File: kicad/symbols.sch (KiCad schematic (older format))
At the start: 70 parts

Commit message: stackup
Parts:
- added logo1306: stackup, servo:layers_stackup, symbol servo:logo
- H1301, H1302, H1303, H1304, H1305, H1306, H1307, H1308, H1309, H1310, H1311, H1312, H1313, H1314, H1315, H1316, H1317, H1318, H1319, H1320, H1321, H1322, H1323, H1324, H1325, H1326, H1327, H1328, H1329, H1330, H1331, H1332, H1333, H1334, H1335, H1336, H1337, H1338, H1339, H1340, H1341, H1342, H1343, H1344, H1345, H1346, H1347, H1348, H1349, H1350, H1351, H1352, H1353, H1354, H1355, H1356, H1357, H1358: price@10 (none) -> 0

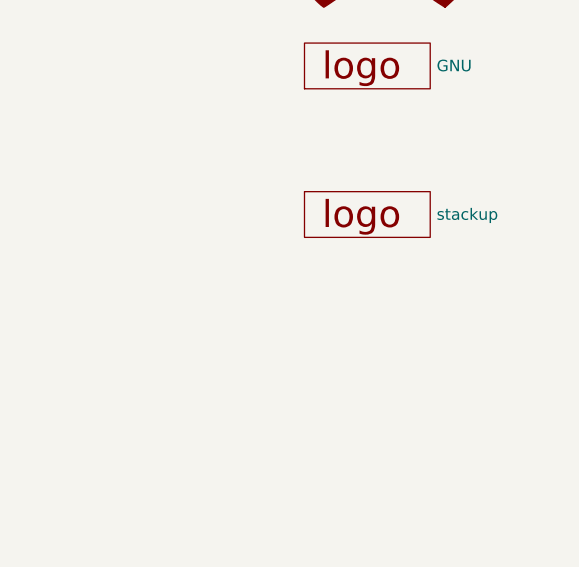
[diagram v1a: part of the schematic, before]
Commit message: changes in footprints
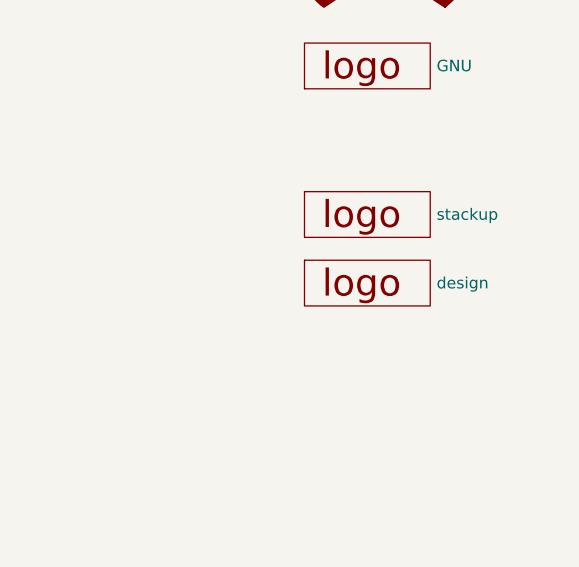
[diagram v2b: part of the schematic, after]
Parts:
- added logo1307: design, servo:layers_design, symbol servo:logo
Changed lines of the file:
@@
+	1    0    0    -1
+$EndComp
+$Comp
+L servo:logo logo1307
+U 1 1 5E5C71DB
+P 13250 6200
+F 0 "logo1307" H 13250 6400 50  0001 C CNN
+F 1 "design" H 13578 6200 50  0000 L CNN
+F 2 "servo:layers_design" H 13250 6200 50  0001 C CNN
+F 3 "~" H 13250 6200 50  0001 C CNN
+F 4 "stackup" H -150 3250 50  0001 C CNN "Description"
+F 5 "-" H -150 3250 50  0001 C CNN "PartNumber"
+F 6 "0" H -150 3250 50  0001 C CNN "price@10"
+	1    13250 6200
 	1    0    0    -1
 $EndComp

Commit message: fine imprivements
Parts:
- H1302, H1304, H1306, H1308: footprint servo:Fiducial_1mm_Dia_2.54mm_Outer_CopperBottom -> servo:Fiducial_1mm_Dia_2.54mm_Outer_CopperTop
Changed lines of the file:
@@
 F 0 "H1302" H 4250 2946 50  0000 L CNN
 F 1 "fiducials" H 4250 2855 50  0000 L CNN
-F 2 "servo:Fiducial_1mm_Dia_2.54mm_Outer_CopperBottom" H 4150 2900 50  0001 C CNN
+F 2 "servo:Fiducial_1mm_Dia_2.54mm_Outer_CopperTop" H 4150 2900 50  0001 C CNN
 F 3 "~" H 4150 2900 50  0001 C CNN
 F 4 "fiducials" H 0   0   50  0001 C CNN "Description"
@@
 F 0 "H1304" H 4950 2946 50  0000 L CNN
 F 1 "fiducials" H 4950 2855 50  0000 L CNN
-F 2 "servo:Fiducial_1mm_Dia_2.54mm_Outer_CopperBottom" H 4850 2900 50  0001 C CNN
+F 2 "servo:Fiducial_1mm_Dia_2.54mm_Outer_CopperTop" H 4850 2900 50  0001 C CNN
 F 3 "~" H 4850 2900 50  0001 C CNN
 F 4 "fiducials" H 0   0   50  0001 C CNN "Description"
@@
 F 0 "H1306" H 5600 2946 50  0000 L CNN
 F 1 "fiducials" H 5600 2855 50  0000 L CNN
-F 2 "servo:Fiducial_1mm_Dia_2.54mm_Outer_CopperBottom" H 5500 2900 50  0001 C CNN
+F 2 "servo:Fiducial_1mm_Dia_2.54mm_Outer_CopperTop" H 5500 2900 50  0001 C CNN
 F 3 "~" H 5500 2900 50  0001 C CNN
 F 4 "fiducials" H 0   0   50  0001 C CNN "Description"
@@
 F 0 "H1308" H 6250 2946 50  0000 L CNN
 F 1 "fiducials" H 6250 2855 50  0000 L CNN
-F 2 "servo:Fiducial_1mm_Dia_2.54mm_Outer_CopperBottom" H 6150 2900 50  0001 C CNN
+F 2 "servo:Fiducial_1mm_Dia_2.54mm_Outer_CopperTop" H 6150 2900 50  0001 C CNN
 F 3 "~" H 6150 2900 50  0001 C CNN
 F 4 "fiducials" H 0   0   50  0001 C CNN "Description"

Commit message: gerbers + pnp + bom ready
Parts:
- removed logo1304: GNU, Symbol:Symbol_GNU-Logo_SilkscreenTop, symbol servo:logo
- added logo1308: pslavkin_top, servo:logo_pslavkin, symbol servo:logo
- logo1302: value pslavkin -> pslavkin_bottom
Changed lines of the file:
@@
 L servo:high_voltage ref1302
 U 1 1 5E38C9D6
-P 13200 3450
-F 0 "ref1302" V 13110 3450 50  0001 C CNN
-F 1 "high_voltage" V 13290 3450 50  0001 C CNN
-F 2 "servo:Symbol_Highvoltage_Type1_CopperTop_Small" H 13400 3950 50  0001 C CNN
-F 3 "~" H 13600 3350 50  0001 C CNN
-F 4 "logo high voltage" H 0   0   50  0001 C CNN "Description"
-F 5 "-" H 0   0   50  0001 C CNN "PartNumber"
-F 6 "0" H 0   0   50  0001 C CNN "price@10"
-	1    13200 3450
+P 13200 3600
+F 0 "ref1302" V 13110 3600 50  0001 C CNN
+F 1 "high_voltage" V 13290 3600 50  0001 C CNN
+F 2 "servo:Symbol_Highvoltage_Type1_CopperTop_Small" H 13400 4100 50  0001 C CNN
+F 3 "~" H 13600 3500 50  0001 C CNN
+F 4 "logo high voltage" H 0   150 50  0001 C CNN "Description"
+F 5 "-" H 0   150 50  0001 C CNN "PartNumber"
+F 6 "0" H 0   150 50  0001 C CNN "price@10"
+	1    13200 3600
 	1    0    0    -1
 $EndComp
@@
 P 13400 2950
 F 0 "logo1302" H 13400 3150 50  0001 C CNN
-F 1 "pslavkin" H 13728 2950 50  0000 L CNN
+F 1 "pslavkin_bottom" H 13728 2950 50  0000 L CNN
 F 2 "servo:logo_pslavkin" H 13400 2950 50  0001 C CNN
 F 3 "~" H 13400 2950 50  0001 C CNN
@@
 L servo:high_voltage ref1303
 U 1 1 5E39D206
-P 13350 3450
-F 0 "ref1303" V 13260 3450 50  0001 C CNN
-F 1 "high_voltage" V 13440 3450 50  0001 C CNN
-F 2 "servo:Symbol_Highvoltage_Type1_CopperTop_Small" H 13550 3950 50  0001 C CNN
-F 3 "~" H 13750 3350 50  0001 C CNN
-F 4 "logo high voltage" H 0   0   50  0001 C CNN "Description"
-F 5 "-" H 0   0   50  0001 C CNN "PartNumber"
-F 6 "0" H 0   0   50  0001 C CNN "price@10"
-	1    13350 3450
+P 13350 3600
+F 0 "ref1303" V 13260 3600 50  0001 C CNN
+F 1 "high_voltage" V 13440 3600 50  0001 C CNN
+F 2 "servo:Symbol_Highvoltage_Type1_CopperTop_Small" H 13550 4100 50  0001 C CNN
+F 3 "~" H 13750 3500 50  0001 C CNN
+F 4 "logo high voltage" H 0   150 50  0001 C CNN "Description"
+F 5 "-" H 0   150 50  0001 C CNN "PartNumber"
+F 6 "0" H 0   150 50  0001 C CNN "price@10"
+	1    13350 3600
 	1    0    0    -1
 $EndComp
@@
 L servo:high_voltage ref1304
 U 1 1 5E39D283
-P 13500 3450
-F 0 "ref1304" V 13410 3450 50  0001 C CNN
-F 1 "high_voltage" V 13590 3450 50  0001 C CNN
-F 2 "servo:Symbol_Highvoltage_Type1_CopperTop_Small" H 13700 3950 50  0001 C CNN
-F 3 "~" H 13900 3350 50  0001 C CNN
-F 4 "logo high voltage" H 0   0   50  0001 C CNN "Description"
-F 5 "-" H 0   0   50  0001 C CNN "PartNumber"
-F 6 "0" H 0   0   50  0001 C CNN "price@10"
-	1    13500 3450
+P 13500 3600
+F 0 "ref1304" V 13410 3600 50  0001 C CNN
+F 1 "high_voltage" V 13590 3600 50  0001 C CNN
+F 2 "servo:Symbol_Highvoltage_Type1_CopperTop_Small" H 13700 4100 50  0001 C CNN
+F 3 "~" H 13900 3500 50  0001 C CNN
+F 4 "logo high voltage" H 0   150 50  0001 C CNN "Description"
+F 5 "-" H 0   150 50  0001 C CNN "PartNumber"
+F 6 "0" H 0   150 50  0001 C CNN "price@10"
+	1    13500 3600
 	1    0    0    -1
 $EndComp
@@
 L servo:high_voltage ref1305
 U 1 1 5E39D300
-P 13650 3450
-F 0 "ref1305" V 13560 3450 50  0001 C CNN
-F 1 "high_voltage" V 13740 3450 50  0001 C CNN
-F 2 "servo:Symbol_Highvoltage_Type1_CopperTop_Small" H 13850 3950 50  0001 C CNN
-F 3 "~" H 14050 3350 50  0001 C CNN
-F 4 "logo high voltage" H 0   0   50  0001 C CNN "Description"
-F 5 "-" H 0   0   50  0001 C CNN "PartNumber"
-F 6 "0" H 0   0   50  0001 C CNN "price@10"
-	1    13650 3450
+P 13650 3600
+F 0 "ref1305" V 13560 3600 50  0001 C CNN
+F 1 "high_voltage" V 13740 3600 50  0001 C CNN
+F 2 "servo:Symbol_Highvoltage_Type1_CopperTop_Small" H 13850 4100 50  0001 C CNN
+F 3 "~" H 14050 3500 50  0001 C CNN
+F 4 "logo high voltage" H 0   150 50  0001 C CNN "Description"
+F 5 "-" H 0   150 50  0001 C CNN "PartNumber"
+F 6 "0" H 0   150 50  0001 C CNN "price@10"
+	1    13650 3600
 	1    0    0    -1
 $EndComp
@@
 	1    13350 4650
 	1    0    0    -1
-$EndComp
-$Comp
-L servo:logo logo1304
-U 1 1 5E3C6E44
-P 13250 5250
-F 0 "logo1304" H 13250 5450 50  0001 C CNN
-F 1 "GNU" H 13578 5250 50  0000 L CNN
-F 2 "Symbol:Symbol_GNU-Logo_SilkscreenTop" H 13250 5250 50  0001 C CNN
-F 3 "~" H 13250 5250 50  0001 C CNN
-F 4 "logo gnu" H 0   0   50  0001 C CNN "Description"
-F 5 "-" H 0   0   50  0001 C CNN "PartNumber"
-F 6 "0" H 0   0   50  0001 C CNN "price@10"
-	1    13250 5250
-	1    0    0    1
 $EndComp
 $Comp
@@
 	1    0    0    -1
 $EndComp
+$Comp
+L servo:logo logo1308
+U 1 1 5E66A127
+P 13400 3200
+F 0 "logo1308" H 13400 3400 50  0001 C CNN
+F 1 "pslavkin_top" H 13728 3200 50  0000 L CNN
+F 2 "servo:logo_pslavkin" H 13400 3200 50  0001 C CNN
+F 3 "~" H 13400 3200 50  0001 C CNN
+F 4 "logo pslavkin" H 0   250 50  0001 C CNN "Description"
+F 5 "-" H 0   250 50  0001 C CNN "PartNumber"
+F 6 "0" H 0   250 50  0001 C CNN "price@10"
+	1    13400 3200
+	1    0    0    -1
+$EndComp

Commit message: some details on gerbers, now released
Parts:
- H1301, H1302, H1303, H1304, H1305, H1306, H1307, H1308, H1309, H1310, H1311, H1312, H1313, H1314, H1315, H1316, H1317, H1318, H1319, H1320, H1321, H1322, H1323, H1324, H1325, H1326, H1327, H1328, H1329, H1330, H1331, H1332, H1333, H1334, H1335, H1336, H1337, H1338, H1339, H1340, H1341, H1342, H1343, H1344, H1345, H1346, H1347, H1348, H1349, H1350, H1351, H1352, H1353, H1354, H1355, H1356, H1357, H1358, LOGO1301, N1301, logo1301, logo1302, logo1303, logo1305, logo1306, logo1307, logo1308, ref1301, ref1302, ref1303, ref1304, ref1305: bom_1 (none) -> 0; bom_2 (none) -> 0; bom_3 (none) -> 0
